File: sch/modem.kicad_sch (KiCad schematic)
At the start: 51 parts, among them J10 TestPoint, J11 TestPoint, J12 TestPoint, J13 TestPoint, J14 TestPoint, J4 Conn_Coaxial, J5 Conn_Coaxial, J6 TestPoint, J7 TestPoint, J8 TestPoint, J9 TestPoint, P1 SF72S006VBAR2500, U1 RC7620_1104625, U2 NX3008NBKW_115, U3 NX3008NBKW_115, U4 NX3008NBKW_115, U5 NX3008NBKW_115, U6 NX3008NBKW_115, U7 NX3008NBKW_115

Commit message: added footprints fore resistors
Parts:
- R11, R12, R13, R3, R4, R5, R6, R7: footprint (none) -> Resistor_SMD:R_0603_1608Metric; MPN (none) -> RC0603FR-0710KL
- R14: footprint (none) -> Resistor_SMD:R_0603_1608Metric; MPN (none) -> RC0603FR-071KL
- R8: footprint (none) -> Resistor_SMD:R_0603_1608Metric; Field5 (none) -> RC0603FR-0710KL
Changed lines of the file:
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@@
 			)
 		)
-		(property "Footprint" ""
+		(property "Footprint" "Resistor_SMD:R_0603_1608Metric"
 			(at 166.37 152.908 90)
 			(effects
@@
 			)
 		)
+		(property "MPN" "RC0603FR-0710KL"
+			(at 166.37 151.13 90)
+			(effects
+				(font
+					(size 1.27 1.27)
+				)
+				(hide yes)
+			)
+		)
 		(pin "1"
 		)
@@
 			)
 		)
-		(property "Footprint" ""
+		(property "Footprint" "Resistor_SMD:R_0603_1608Metric"
 			(at 165.862 110.49 90)
 			(effects
@@
 			)
 		)
+		(property "MPN" "RC0603FR-0710KL"
+			(at 167.64 110.49 0)
+			(effects
+				(font
+					(size 1.27 1.27)
+				)
+				(hide yes)
+			)
+		)
 		(pin "2"
 		)
@@
 			)
 		)
-		(property "Footprint" ""
+		(property "Footprint" "Resistor_SMD:R_0603_1608Metric"
 			(at 165.862 87.63 90)
 			(effects
@@
 			)
 		)
+		(property "MPN" "RC0603FR-0710KL"
+			(at 167.64 87.63 0)
+			(effects
+				(font
+					(size 1.27 1.27)
+				)
+				(hide yes)
+			)
+		)
 		(pin "2"
 		)
@@
 			)
 		)
-		(property "Footprint" ""
+		(property "Footprint" "Resistor_SMD:R_0603_1608Metric"
 			(at 165.862 132.08 90)
 			(effects
@@
 			)
 		)
+		(property "MPN" "RC0603FR-0710KL"
+			(at 167.64 132.08 0)
+			(effects
+				(font
+					(size 1.27 1.27)
+				)
+				(hide yes)
+			)
+		)
 		(pin "1"
 		)
@@
 			)
 		)
-		(property "Footprint" ""
+		(property "Footprint" "Resistor_SMD:R_0603_1608Metric"
 			(at 240.03 108.458 90)
 			(effects
@@
 			)
 		)
+		(property "MPN" "RC0603FR-071KL"
+			(at 240.03 106.68 90)
+			(effects
+				(font
+					(size 1.27 1.27)
+				)
+				(hide yes)
+			)
+		)
 		(pin "1"
 		)
@@
 			)
 		)
-		(property "Footprint" ""
+		(property "Footprint" "Resistor_SMD:R_0603_1608Metric"
 			(at 240.03 75.438 90)
 			(effects
@@
 			)
 		)
+		(property "MPN" "RC0603FR-0710KL"
+			(at 240.03 73.66 90)
+			(effects
+				(font
+					(size 1.27 1.27)
+				)
+				(hide yes)
+			)
+		)
 		(pin "1"
 		)
@@
 			)
 		)
-		(property "Footprint" ""
+		(property "Footprint" "Resistor_SMD:R_0603_1608Metric"
 			(at 229.362 119.38 90)
 			(effects
@@
 			)
 		)
+		(property "MPN" "RC0603FR-0710KL"
+			(at 231.14 119.38 0)
+			(effects
+				(font
+					(size 1.27 1.27)
+				)
+				(hide yes)
+			)
+		)
 		(pin "2"
 		)
@@
 			)
 		)
-		(property "Footprint" ""
+		(property "Footprint" "Resistor_SMD:R_0603_1608Metric"
 			(at 172.212 154.94 90)
 			(effects
@@
 			)
 		)
+		(property "MPN" "RC0603FR-0710KL"
+			(at 173.99 154.94 0)
+			(effects
+				(font
+					(size 1.27 1.27)
+				)
+				(hide yes)
+			)
+		)
 		(pin "1"
 		)
@@
 			)
 		)
-		(property "Footprint" ""
+		(property "Footprint" "Resistor_SMD:R_0603_1608Metric"
 			(at 229.362 86.36 90)
 			(effects
@@
 			)
 		)
+		(property "MPN" "RC0603FR-0710KL"
+			(at 231.14 86.36 0)
+			(effects
+				(font
+					(size 1.27 1.27)
+				)
+				(hide yes)
+			)
+		)
 		(pin "2"
 		)
@@
 			)
 		)
-		(property "Footprint" ""
+		(property "Footprint" "Resistor_SMD:R_0603_1608Metric"
 			(at 193.802 22.86 90)
 			(effects
@@
 			(at 195.58 22.86 0)
 			(effects
+				(font
+					(size 1.27 1.27)
+				)
+				(hide yes)
+			)
+		)
+		(property "Field5" "RC0603FR-0710KL"
+			(at 195.58 22.86 0)
+			(effects

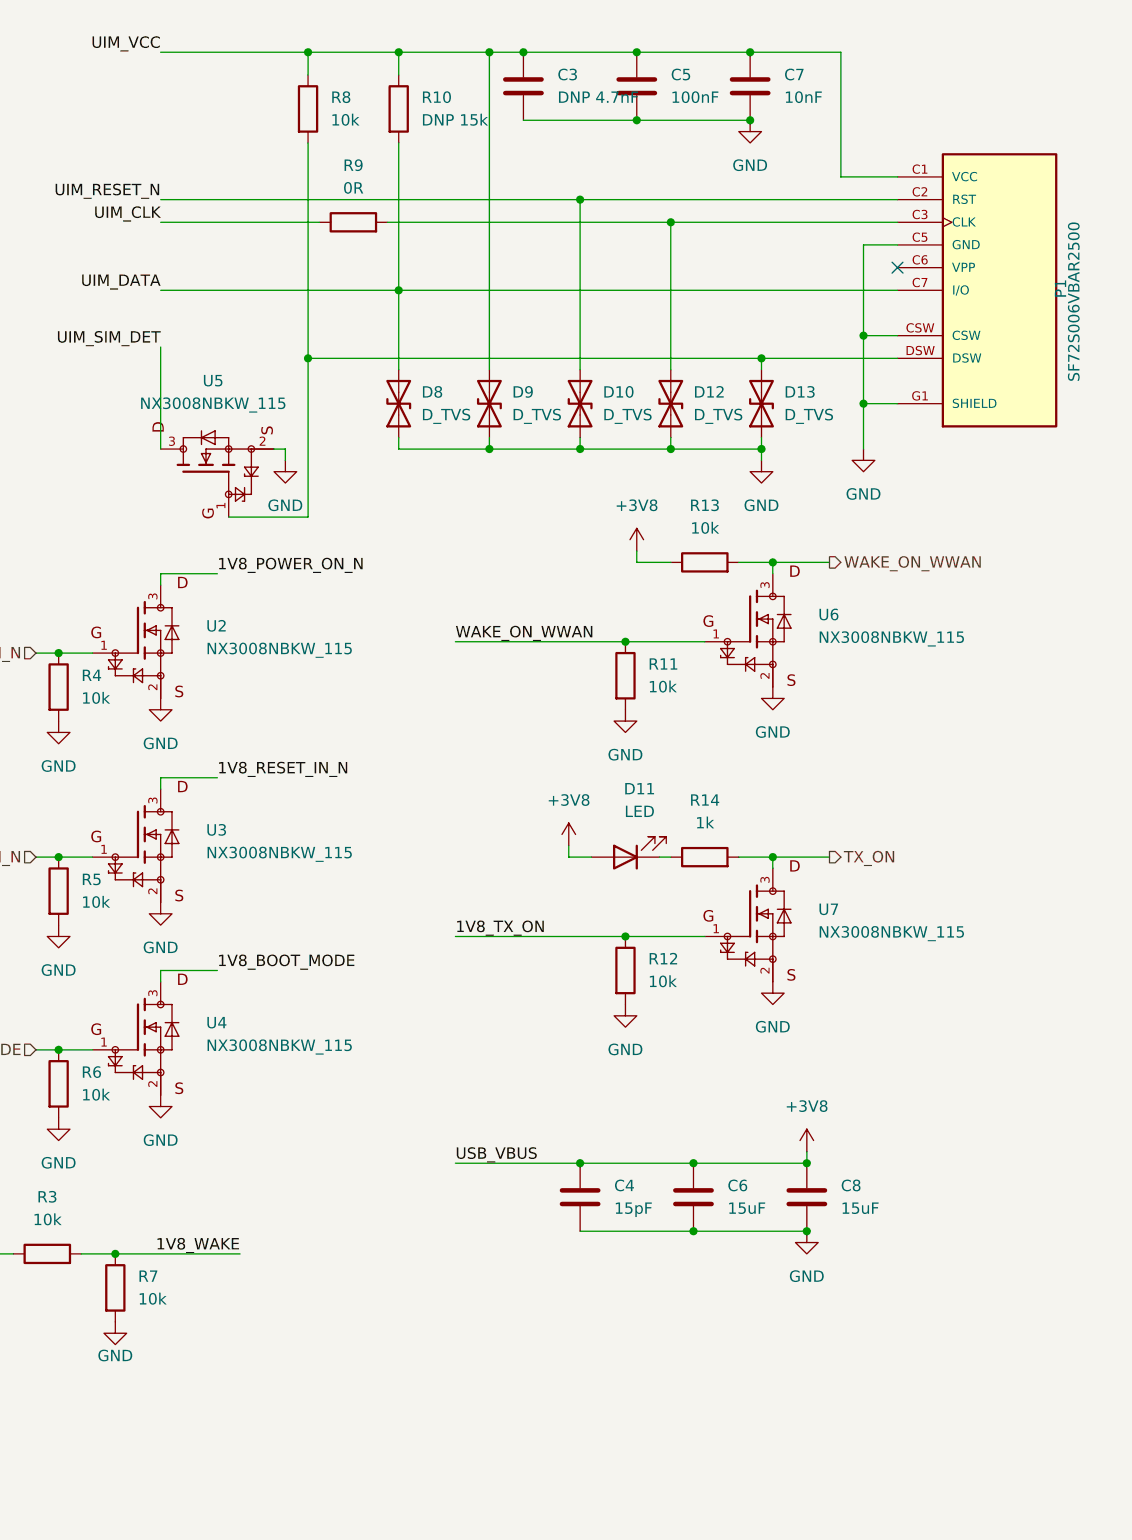
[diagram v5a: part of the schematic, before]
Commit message: Added footprints for diodes in modem
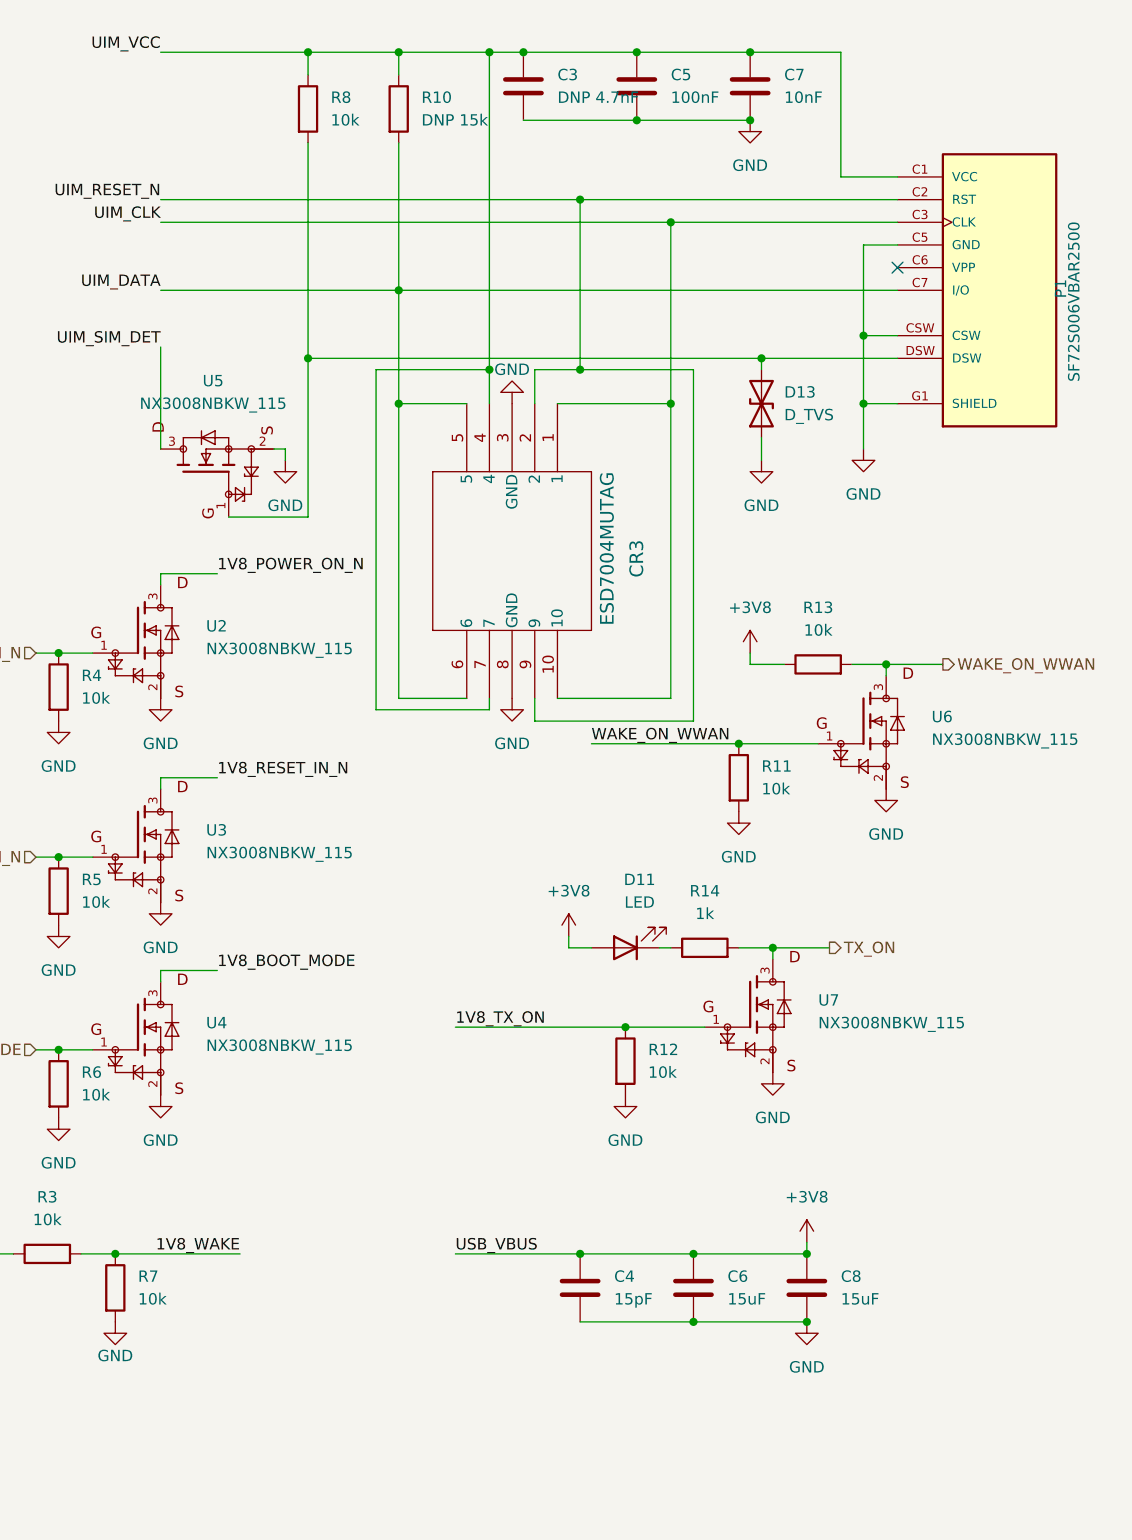
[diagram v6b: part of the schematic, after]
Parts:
- removed D10, D12, D8, D9: D_TVS, symbol Device:D_TVS
- removed R9: 0R, symbol Device:R
- added CR3: ESD7004MUTAG, UDFN10_517BB_ONS, symbol ESD7004MUTAG:ESD7004MUTAG
- C3: footprint (none) -> Capacitor_SMD:C_0603_1608Metric
- D13, D6, D7: footprint (none) -> Diode_SMD:D_0402_1005Metric; MPN (none) -> ESD7004MUTAG
- J10, J11, J12, J13, J14, J6, J7, J8, J9, TP1, TP2, TP3, TP4, TP5, TP6: footprint (none) -> TestPoint:TestPoint_Loop_D2.50mm_Drill1.85mm
- R10: footprint (none) -> Resistor_SMD:R_0603_1608Metric
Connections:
- net GND: now also CR3.3 (GND), CR3.8 (GND)
- net UIM_CLK: now also P1.C3 (CLK), CR3.1, CR3.10
- net UIM_DATA: now also CR3.5, CR3.6
- net UIM_RESET_N: now also CR3.2, CR3.9
- net UIM_VCC: now also CR3.4, CR3.7
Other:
- moved on the sheet: C4, C6, C8, D11, R11, R12, R13, R14, U6, U7

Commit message: added more footprinst and esd
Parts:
- D11: footprint (none) -> LTST-C190GKT:LEDM1608X80; MPN (none) -> LTST-C190GKT
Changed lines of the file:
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@@
 			)
 		)
-		(property "Footprint" ""
+		(property "Footprint" "LTST-C190GKT:LEDM1608X80"
 			(at 231.14 116.84 0)
 			(effects
@@
 			(at 231.14 116.84 0)
 			(effects
+				(font
+					(size 1.27 1.27)
+				)
+				(hide yes)
+			)
+		)
+		(property "MPN" "LTST-C190GKT"
+			(at 231.14 116.84 0)
+			(effects

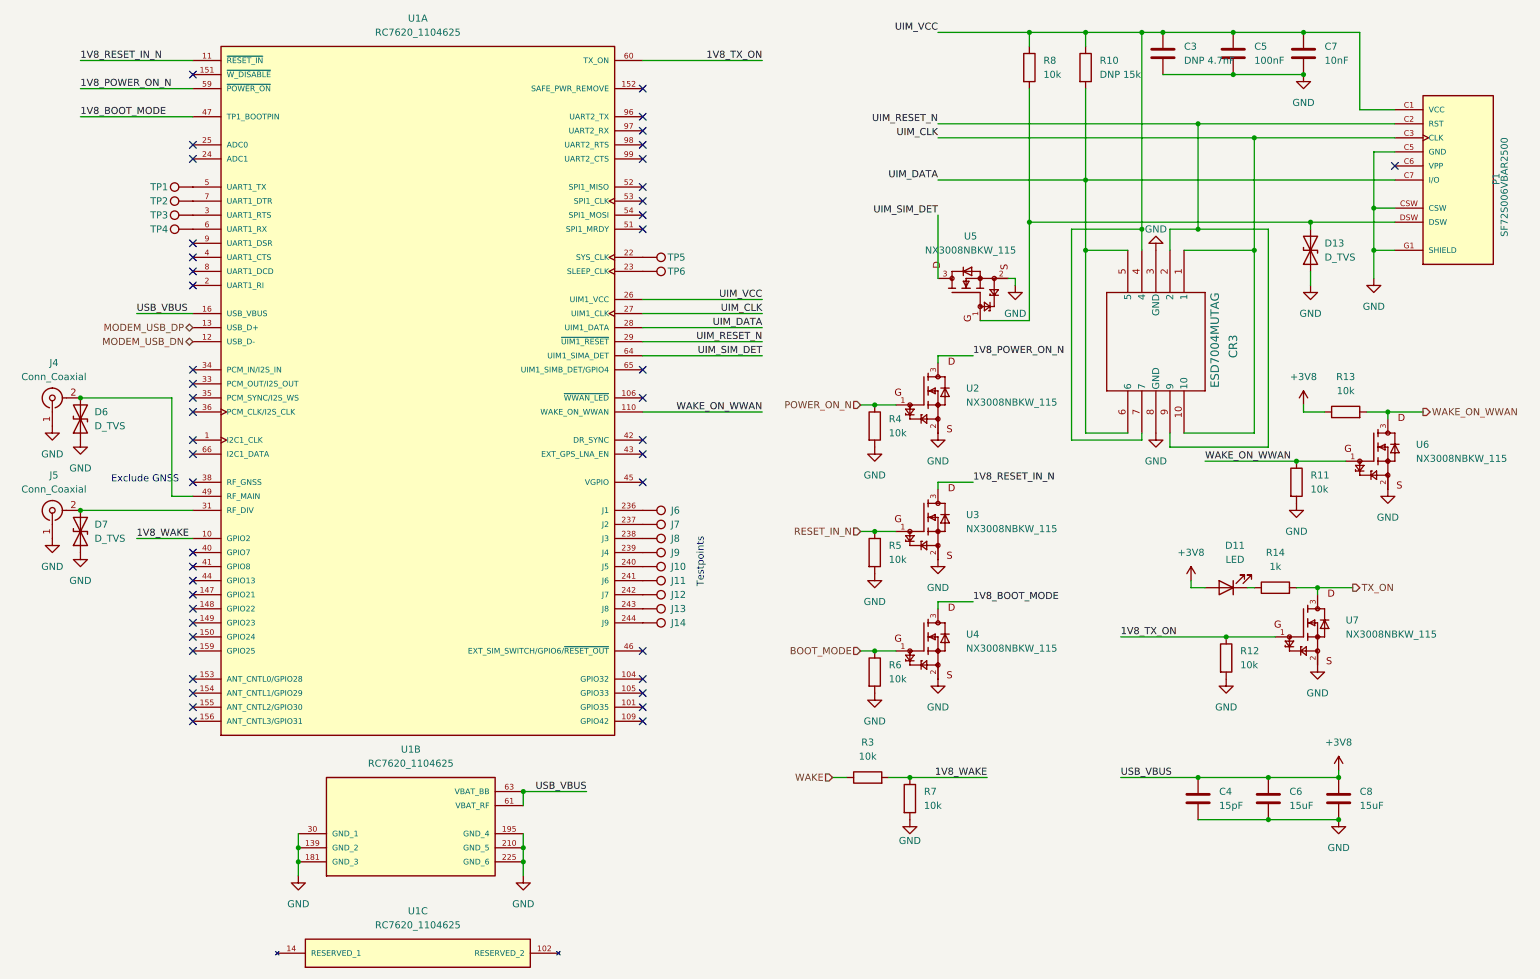
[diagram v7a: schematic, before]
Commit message: added more footprints and added to pcb
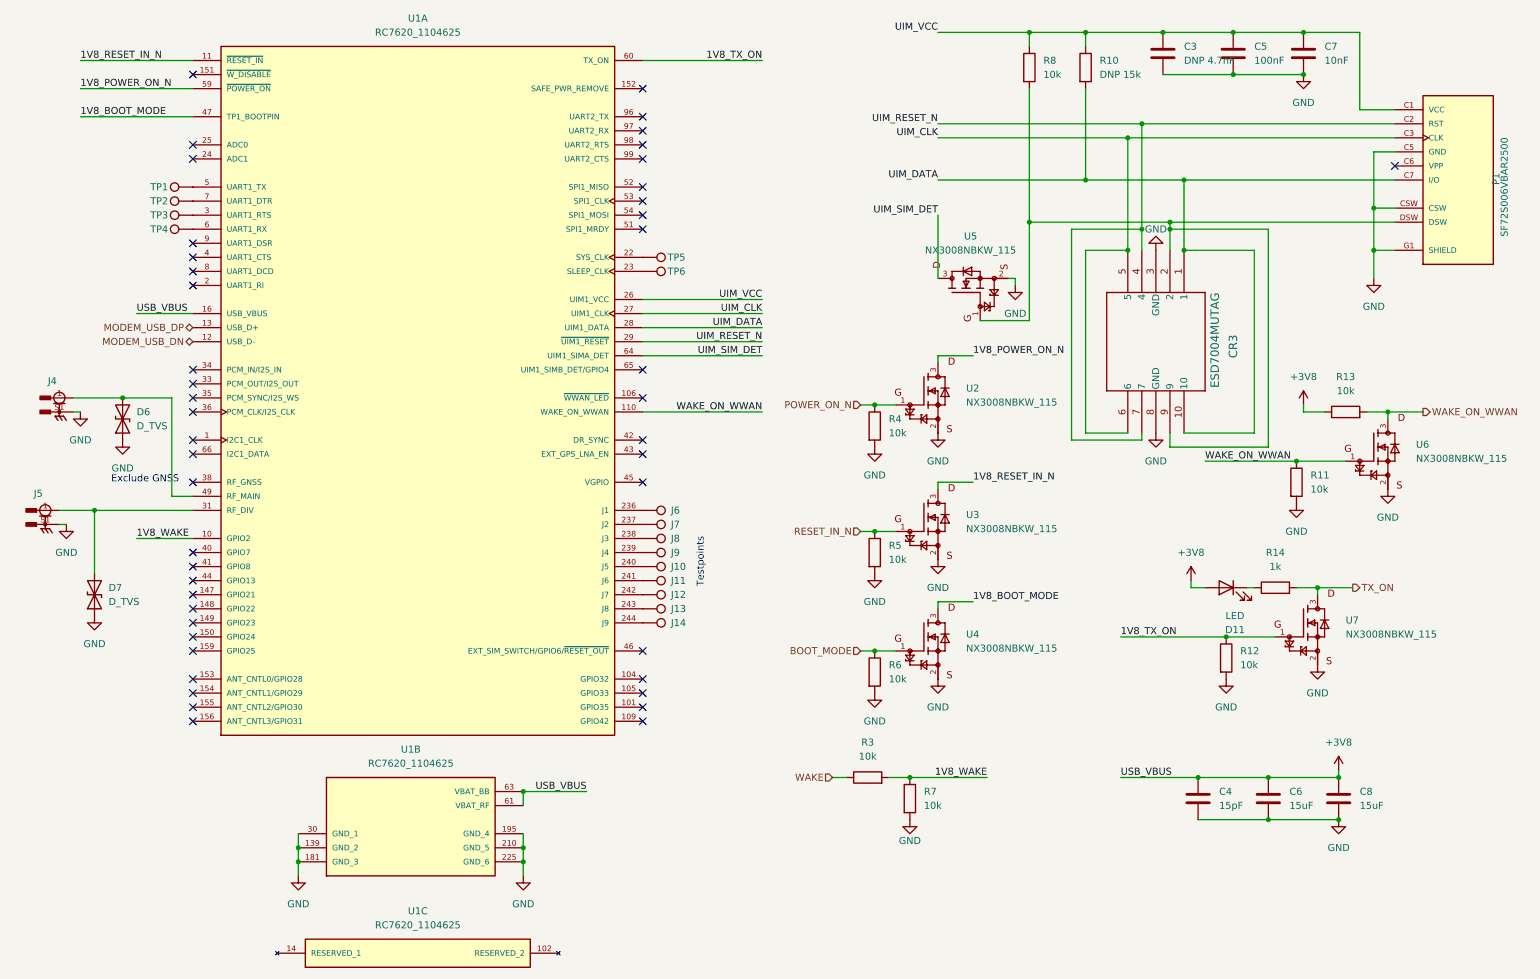
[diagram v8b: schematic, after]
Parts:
- removed D13: D_TVS, Diode_SMD:D_0402_1005Metric, symbol Device:D_TVS
- removed J4, J5: Conn_Coaxial, symbol Connector:Conn_Coaxial
- added J4, J5: CONMHF1-SMD-G-T, CONMHF1-SMD-G-T:LINX_CONMHF1-SMD-G-T, symbol CONMHF1-SMD-G-T:CONMHF1-SMD-G-T
- D6, D7: MPN ESD7004MUTAG -> 0402ESDA-MLP1
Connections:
- net GND: now also J4.S1, J4.S2, J4.S3, J5.S1, J5.S2, J5.S3
- net UIM_CLK: now also CR3.5, CR3.6; no longer CR3.1, CR3.10
- net UIM_DATA: now also CR3.1, CR3.10; no longer CR3.5, CR3.6
- net UIM_RESET_N: now also CR3.4, CR3.7; no longer CR3.2, CR3.9
- net UIM_VCC: no longer CR3.4, CR3.7
- net at P1.DSW, R8.2, U5.1: now also CR3.2, CR3.9
- net at D7.2 (A2), U1.31 (RF_DIV): now also J5.1
- net at D6.2 (A2), U1.49 (RF_MAIN): now also J4.1
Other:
- moved on the sheet: D11, D6, D7
